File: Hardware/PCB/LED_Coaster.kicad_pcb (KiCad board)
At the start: 2 copper layers, 90 x 90 mm, 67 parts, among them J1 Li-po, J3 USB_C_Receptacle_USB2.0_16P, J4 UART, SW1 SW_SPDT, U1 ESP32-C3-WROOM-02-H4, U3 MCP73831-2-OT, U4 AMS1117-3.3

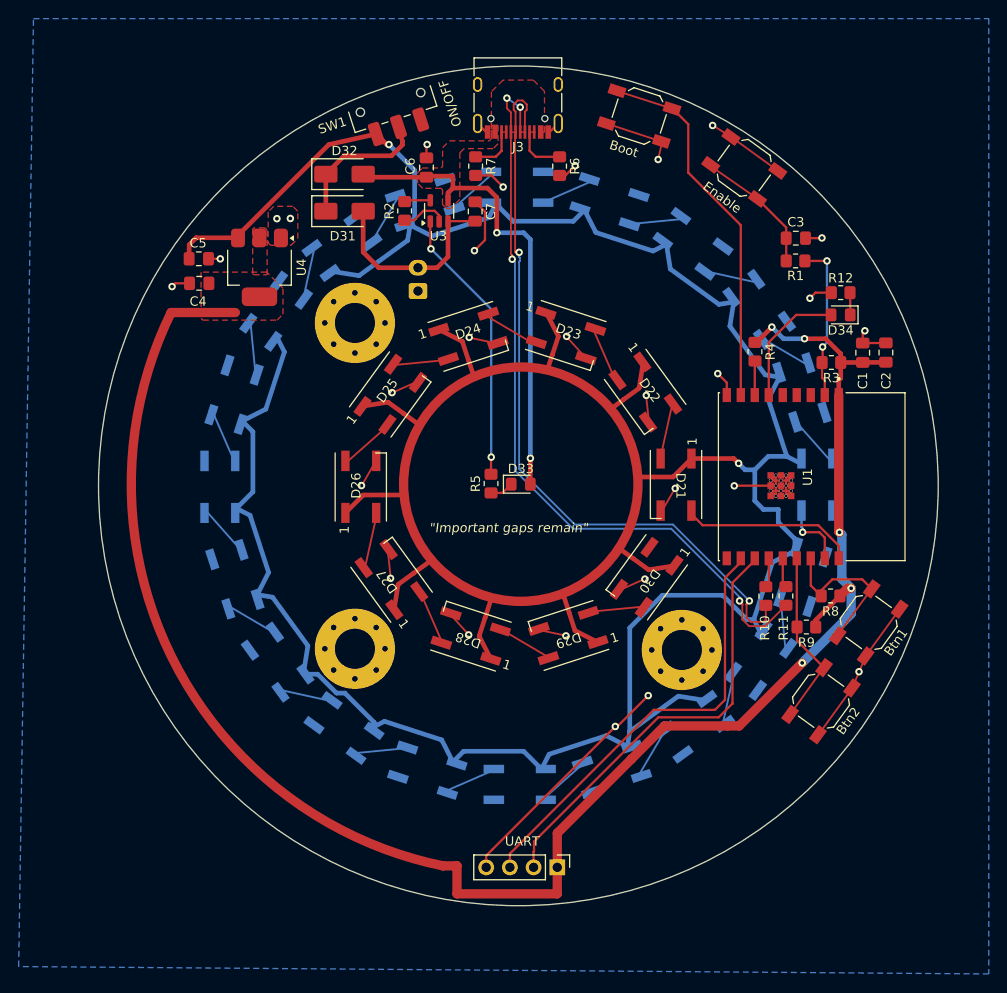
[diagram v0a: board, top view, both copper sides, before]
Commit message: Verify F8 result; correct Phase 3 and rescope Phase 5
Analysed the post-F8 board net by net.

Phase 2 verified: footprint swaps landed, D31/D32 gone, DNP cleared on
D1-D30 and U1 with MPNs intact, 88 parts in both schematic and PCB, and
total copper unchanged at 413 items so no routing was lost. Corrected the
predicted count from 19 added to the actual 23 (C8-C19 were undercounted).

Phase 3 corrected. It said to delete the old +BATT traces feeding the
rings; that would have been destructive. KiCad re-assigned those 104
copper items from +BATT to +LED_PWR automatically during F8 because the
pads they attach to changed net. Only 29 stale items actually need
deleting, all on an empty net in x 129-147, y 42-79.

Phase 5 rescoped: 38 nets need routing, 28 of them LED data links that
were never routed in this file. Confirmed pre-existing by checking the
previous commit - the data nets had zero copper there too.

Decoupling cap advice reversed: 8 of C8-C19 now go on the back beside
their LEDs. The front-only placement existed to avoid double-sided
assembly, which is no longer a constraint.

Co-Authored-By: Claude Opus 5 <noreply@anthropic.com>
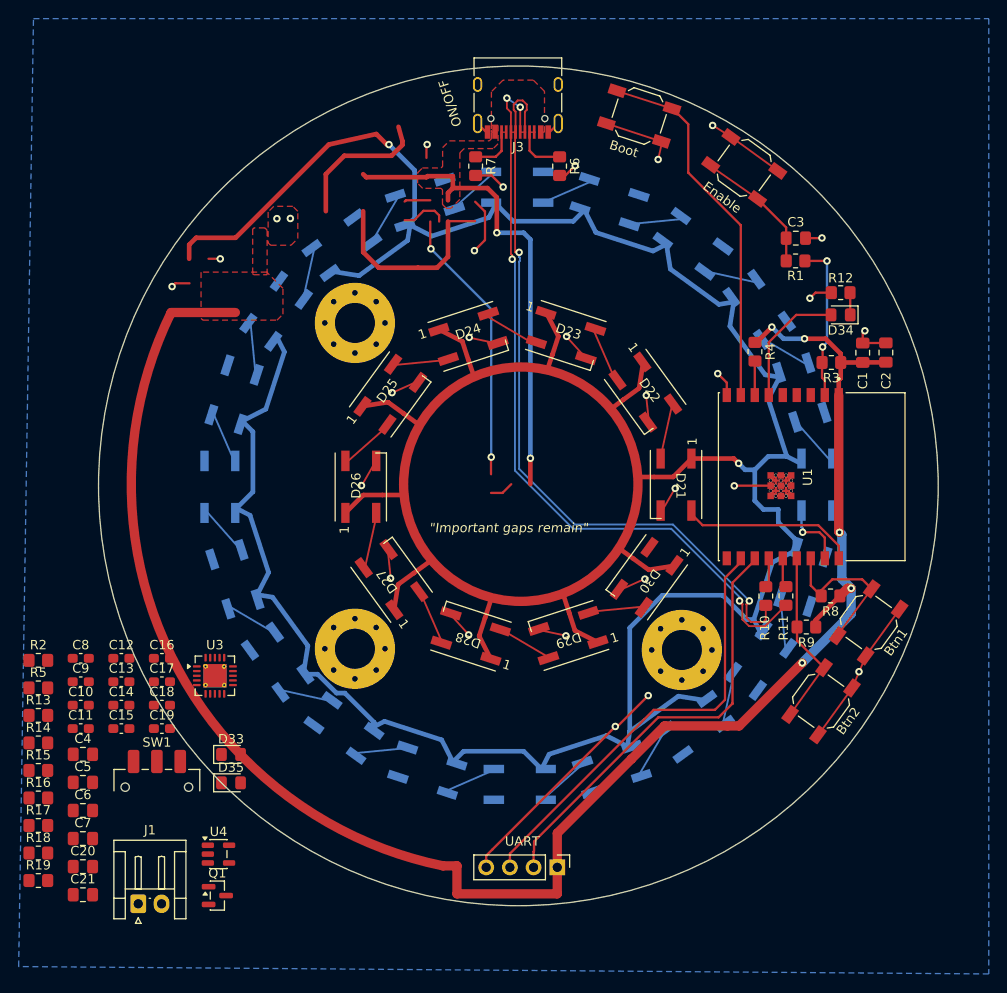
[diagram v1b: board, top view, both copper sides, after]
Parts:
- removed D31, D32: SS34, Diode_SMD:D_SMA
- added C10: 100nF, Capacitor_SMD:C_0603_1608Metric_Pad1.08x0.95mm_HandSolder, F.Cu at (103.1, 103.5)
- added C11: 100nF, Capacitor_SMD:C_0603_1608Metric_Pad1.08x0.95mm_HandSolder, F.Cu at (103.1, 106.0)
- added C12: 100nF, Capacitor_SMD:C_0603_1608Metric_Pad1.08x0.95mm_HandSolder, F.Cu at (107.4, 98.5)
- added C13: 100nF, Capacitor_SMD:C_0603_1608Metric_Pad1.08x0.95mm_HandSolder, F.Cu at (107.4, 101.0)
- added C14: 100nF, Capacitor_SMD:C_0603_1608Metric_Pad1.08x0.95mm_HandSolder, F.Cu at (107.4, 103.5)
- added C15: 100nF, Capacitor_SMD:C_0603_1608Metric_Pad1.08x0.95mm_HandSolder, F.Cu at (107.4, 106.0)
- added C16: 100nF, Capacitor_SMD:C_0603_1608Metric_Pad1.08x0.95mm_HandSolder, F.Cu at (111.8, 98.5)
- added C17: 100nF, Capacitor_SMD:C_0603_1608Metric_Pad1.08x0.95mm_HandSolder, F.Cu at (111.8, 101.0)
- added C18: 100nF, Capacitor_SMD:C_0603_1608Metric_Pad1.08x0.95mm_HandSolder, F.Cu at (111.8, 103.5)
- added C19: 100nF, Capacitor_SMD:C_0603_1608Metric_Pad1.08x0.95mm_HandSolder, F.Cu at (111.8, 106.0)
- added C20: 22uF, Capacitor_SMD:C_0805_2012Metric_Pad1.18x1.45mm_HandSolder, F.Cu at (103.3, 120.8)
- added C21: 0.1uF, Capacitor_SMD:C_0805_2012Metric_Pad1.18x1.45mm_HandSolder, F.Cu at (103.3, 123.8)
- added C8: 100nF, Capacitor_SMD:C_0603_1608Metric_Pad1.08x0.95mm_HandSolder, F.Cu at (103.1, 98.5)
- added C9: 100nF, Capacitor_SMD:C_0603_1608Metric_Pad1.08x0.95mm_HandSolder, F.Cu at (103.1, 101.0)
- added D35: LED, LED_SMD:LED_0805_2012Metric_Pad1.15x1.40mm_HandSolder, F.Cu at (119.2, 111.8)
- added Q1: AO3401A, Package_TO_SOT_SMD:SOT-23, F.Cu at (117.7, 123.9)
- added R13: 100k, Resistor_SMD:R_0805_2012Metric_Pad1.20x1.40mm_HandSolder, F.Cu at (98.5, 104.6)
- added R14: 10k, Resistor_SMD:R_0805_2012Metric_Pad1.20x1.40mm_HandSolder, F.Cu at (98.5, 107.6)
- added R15: 20k, Resistor_SMD:R_0805_2012Metric_Pad1.20x1.40mm_HandSolder, F.Cu at (98.5, 110.5)
- added R16: 1k, Resistor_SMD:R_0805_2012Metric_Pad1.20x1.40mm_HandSolder, F.Cu at (98.5, 113.5)
- added R17: 100k, Resistor_SMD:R_0805_2012Metric_Pad1.20x1.40mm_HandSolder, F.Cu at (98.5, 116.4)
- added R18: 470k, Resistor_SMD:R_0805_2012Metric_Pad1.20x1.40mm_HandSolder, F.Cu at (98.5, 119.4)
- added R19: 470k, Resistor_SMD:R_0805_2012Metric_Pad1.20x1.40mm_HandSolder, F.Cu at (98.5, 122.3)
- C4: value 2.2uF -> 4.7uF
- J1: moved to F.Cu
- U3: value MCP73831-2-OT -> MCP73871-2CC; footprint Package_TO_SOT_SMD:SOT-23-5 -> Package_DFN_QFN:QFN-20-1EP_4x4mm_P0.5mm_EP2.5x2.5mm_ThermalVias
- U4: value AMS1117-3.3 -> TLV75533PDBVR; footprint Package_TO_SOT_SMD:SOT-223-3_TabPin2 -> Package_TO_SOT_SMD:SOT-23-5
- moved C7 79.3 mm to (103.3, 117.8), turned to 0 degrees
- moved C6 78.1 mm to (103.3, 114.8), turned to 0 degrees
- moved SW1 77.6 mm to (111.3, 112.3), turned to 0 degrees
- moved J1 72.2 mm to (109.3, 124.8), turned to 0 degrees
- moved U4 63.0 mm to (117.9, 119.5), turned to 0 degrees
- moved R2 62.1 mm to (98.5, 98.7), turned to 0 degrees
- moved U3 55.3 mm to (117.5, 100.4), turned to 0 degrees
- moved C5 54.9 mm to (103.3, 111.8)
- moved C4 54.5 mm to (103.3, 108.8), turned to 0 degrees
- moved R5 53.2 mm to (98.5, 101.7), turned to 0 degrees
- moved D33 42.5 mm to (119.2, 108.8)
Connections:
- C4 pad 1: GND -> +SYS
- C4 pad 2: +BATT -> GND
- C5 pad 1: GND -> +3V3
- C5 pad 2: +3V3 -> GND
- C6 pad 1: GND -> +5V
- C6 pad 2: +5V -> GND
- C7 pad 1: GND -> +BATT
- C7 pad 2: Net-(D31-A) -> GND
- D1 pad 1: +BATT -> +LED_PWR
- D10 pad 1: +BATT -> +LED_PWR
- D11 pad 1: +BATT -> +LED_PWR
- D12 pad 1: +BATT -> +LED_PWR
- D13 pad 1: +BATT -> +LED_PWR
- D14 pad 1: +BATT -> +LED_PWR
- D15 pad 1: +BATT -> +LED_PWR
- D16 pad 1: +BATT -> +LED_PWR
- D17 pad 1: +BATT -> +LED_PWR
- D18 pad 1: +BATT -> +LED_PWR
- D19 pad 1: +BATT -> +LED_PWR
- D2 pad 1: +BATT -> +LED_PWR
- D20 pad 1: +BATT -> +LED_PWR
- D21 pad 1: +BATT -> +LED_PWR
- D22 pad 1: +BATT -> +LED_PWR
- D23 pad 1: +BATT -> +LED_PWR
- D24 pad 1: +BATT -> +LED_PWR
- D25 pad 1: +BATT -> +LED_PWR
- D26 pad 1: +BATT -> +LED_PWR
- D27 pad 1: +BATT -> +LED_PWR
- D28 pad 1: +BATT -> +LED_PWR
- D29 pad 1: +BATT -> +LED_PWR
- D3 pad 1: +BATT -> +LED_PWR
- D30 pad 1: +BATT -> +LED_PWR
- D4 pad 1: +BATT -> +LED_PWR
- D5 pad 1: +BATT -> +LED_PWR
- D6 pad 1: +BATT -> +LED_PWR
- D7 pad 1: +BATT -> +LED_PWR
- D8 pad 1: +BATT -> +LED_PWR
- D9 pad 1: +BATT -> +LED_PWR
- J1 pad 2: Net-(D31-A) -> +BATT
- R2 pad 1: Net-(U3-PROG) -> Net-(U3-PROG1)
- R2 pad 2: Net-(U3-V_{SS}) -> GND
- R5 pad 1: Net-(D33-K) -> Net-(U3-STAT1/~{LBO})
- R5 pad 2: Net-(U3-STAT) -> Net-(D33-K)
- SW1 pad 2: Net-(D31-K) -> GND
- SW1 pad 3: +BATT -> Net-(Q1-G)
- U1 pad 3: unconnected-(U1-IO4-Pad3) -> /BAT_SENSE
- U3 pad 1: Net-(U3-STAT) -> +SYS
- U3 pad 2: Net-(U3-V_{SS}) -> +5V
- U3 pad 3: Net-(D31-A) -> GND
- U3 pad 4: +5V -> +SYS
- U3 pad 5: Net-(U3-PROG) -> Net-(U3-THERM)
- U4 pad 1: GND -> +SYS
- U4 pad 2: +3V3 -> GND
- U4 pad 3: +BATT -> +LED_PWR
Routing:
- net +LED_PWR: track 0.00 -> 318.8 mm, vias 0 -> 2
- net +BATT: track 318.8 -> 0.00 mm, vias 2 -> 0
- net (no net): track 0.00 -> 74.4 mm, vias 0 -> 2
- net Net-(U3-STAT): track 29.8 -> 0.00 mm, vias 2 -> 0
- net Net-(D31-A): track 21.4 -> 0.00 mm
- net Net-(D31-K): track 15.5 -> 0.00 mm
- net Net-(U3-V_{SS}): track 4.98 -> 0.00 mm
- net Net-(U3-PROG): track 2.80 -> 0.00 mm

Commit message: Phase 3: delete the orphaned copper from the old power section
The 29 netless copper items left behind by D31/D32 and the old U3/U4
footprints are removed. Total board copper goes 413 -> 384; nothing else
changed. +LED_PWR keeps its 104-item ring distribution, GND 92, the ring
inputs, USB and buttons untouched, 88 footprints, antenna keepout intact.
No netless copper remains.

ORDERING.md corrections found while verifying readiness:

- Phase 3 lists the exact bounding box and the 25 F.Cu / 2 via / 2 B.Cu
  breakdown, and now says to select by net rather than rubber-banding an
  area that also holds live +5V, GND and +LED_PWR copper. A new box says
  to leave the netless ESP32 antenna keepout zone alone.
- Phase 4 said "SW1 - leave it where it is". F8 moved the entire power
  section off the board, SW1 included, because the section was redrawn in
  the schematic. Phase 4 now lists the 28 off-board footprints and the
  pre-F8 positions worth reusing, and gains placement boxes for J1 and
  D33, which it previously referenced but never told you to place.
- Phase 8 expected 27 BOM lines; the schematic yields 26 for 83 parts.
- The v10 format upgrade box is ticked - it landed inside e196df2.

Co-Authored-By: Claude Opus 5 <noreply@anthropic.com>
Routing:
- net (no net): track 74.4 -> 0.00 mm, vias 2 -> 0

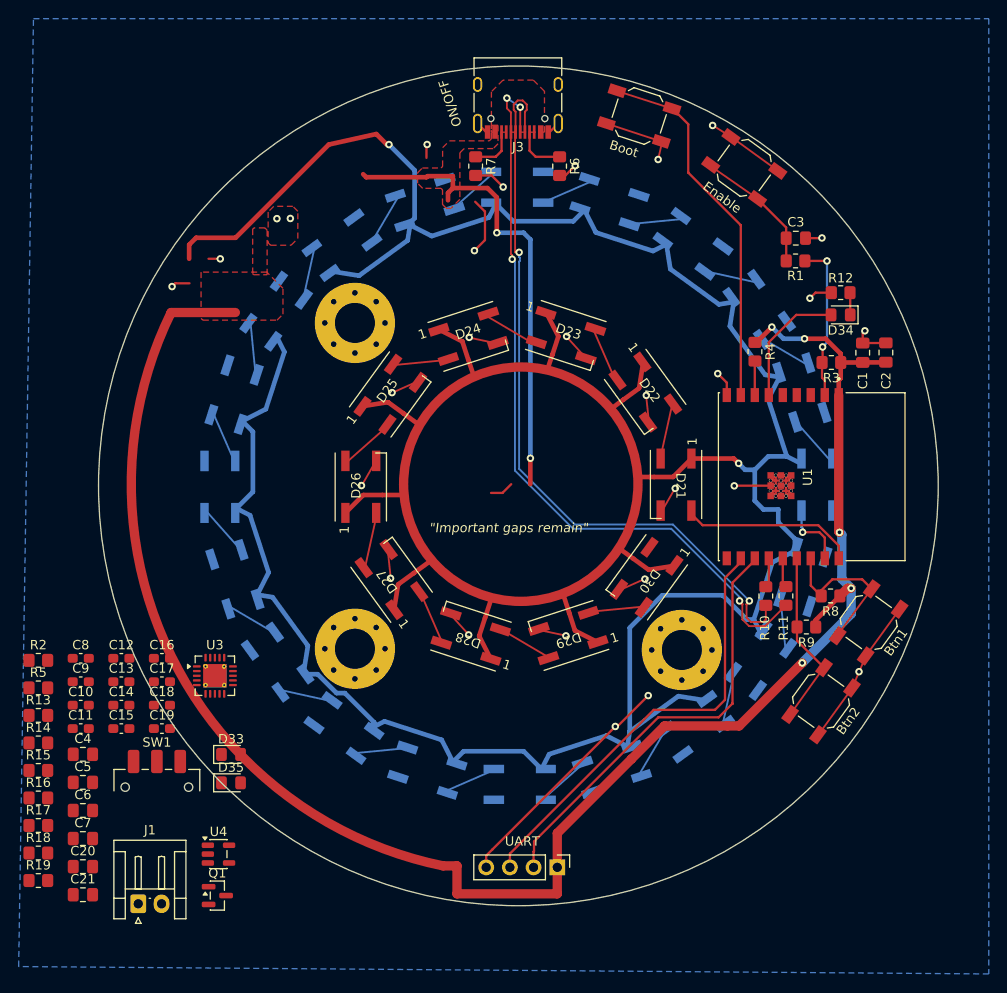
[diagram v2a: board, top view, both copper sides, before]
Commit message: Phase 4: place all 34 parts, and correct the outer-ring rotation analysis
Every unplaced part now has a verified position, angle and side. Checked
against the board file: courtyard overlap per side, through-hole pads against
the opposite side, all four corners inside the 90 mm outline, and every pad
against tracks of a foreign net.

Before placing, 13 more leftovers went: 7 thin +LED_PWR feed segments from the
old switch run and 4 GND segments plus 2 vias from the old C4/C5 connections.
Phase 3 could not catch these because they still carried a live net. Copper is
371 items. Three dead copper zones also went - two +3V3 and one GND, drawn
around the old AMS1117 at (122.25, 56.58), each connecting to zero pads of its
own net and each sitting on top of the new charger. 15 zones remain.

Two placement decisions differ from what this file said before:

- The status LEDs D33/D35 and their resistors moved from the centre of the
  front face to the back, outside the LED ring, 10 mm from the USB-C port. The
  front face is almost hidden in the enclosure.
- The battery-sense divider R18/R19 groups with C21 at the ESP32 rather than at
  the battery, so the 235k divider node stays short and +BATT takes the long
  run instead.

Corrected: the outer ring D1-D20 is not uniformly oriented. An earlier revision
here claimed both rings held their angle to 0.1°, measured with rot + bearing.
That is the right invariant on the front and the wrong one on a mirrored layer.
Measured with rot - bearing the outer ring spreads 324° - it carries front-side
rotations while the parts sit on the back, fanning through 5 orientations 36°
apart. Pre-existing and identical in the previously fabricated board. Not worth
fixing: re-rotating all 20 would give uniform 5.5 mm data hops instead of
4-16 mm, but collides with H1/H3/H4, J1, C10 and C14.

That fan is why the decoupling caps take rot = -bearing on both sides rather
than a radial rule. It holds each cap at a fixed angle to its neighbouring LEDs
- 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
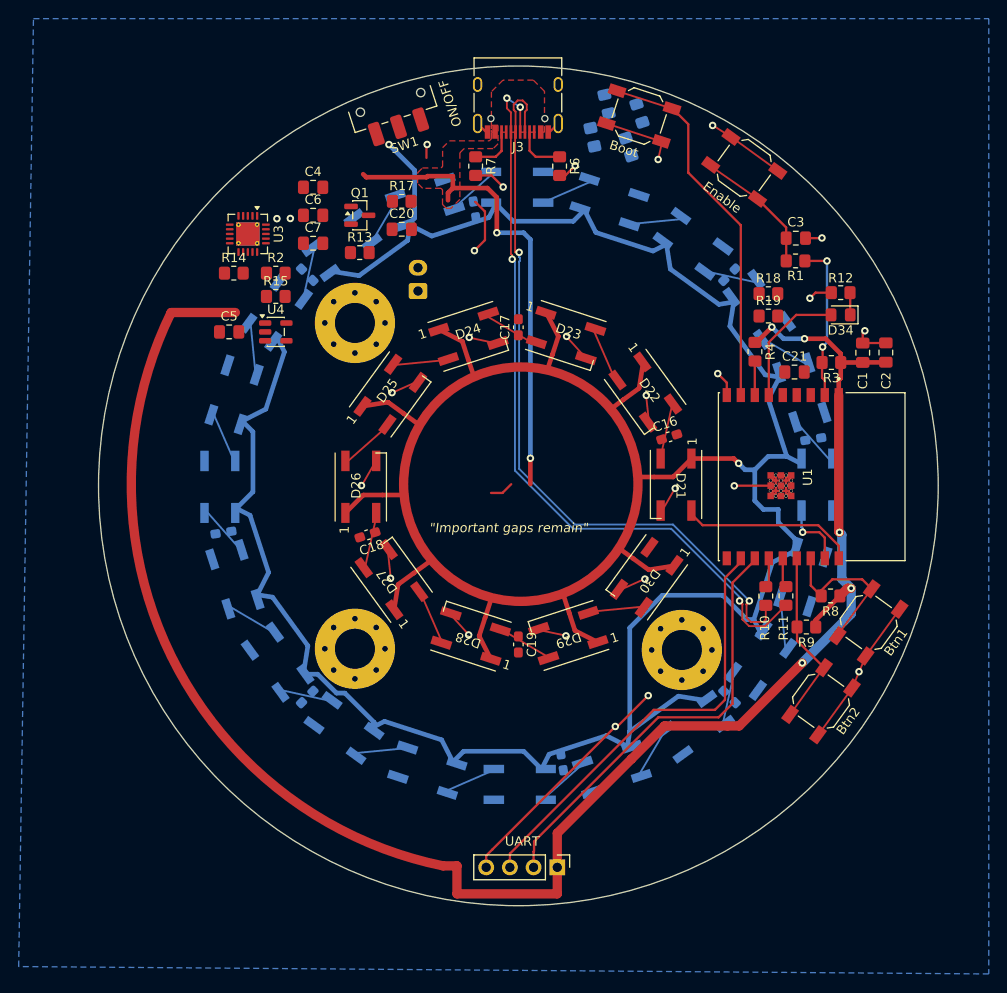
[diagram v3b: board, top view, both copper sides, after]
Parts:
- C10, C11, C12, C13, C14, C15, C8, C9, D33, D35, J1, R16, R5: moved to B.Cu
- moved R19 98.9 mm to (176.8, 61.8)
- moved R18 98.6 mm to (176.8, 59.4)
- moved C21 94.6 mm to (179.6, 67.8)
- moved R16 94.2 mm to (161.8, 43.7), turned to 108 degrees
- moved D35 84.1 mm to (163.0, 40.1), turned to 108 degrees
- moved R5 83.7 mm to (157.9, 42.6), turned to 102 degrees
- moved C9 82.1 mm to (172.6, 57.4), turned to 45 degrees
- moved C8 82.0 mm to (181.6, 75.0), turned to 9 degrees
- moved D33 80.5 mm to (159.4, 39.1), turned to 103 degrees
- moved SW1 77.6 mm to (136.3, 38.9), turned to -162 degrees
- moved R17 77.4 mm to (137.5, 49.5)
- moved C20 76.4 mm to (137.5, 52.5)
- moved Q1 74.5 mm to (133.0, 51.0)
- moved J1 72.2 mm to (139.2, 59.1), turned to 90 degrees
- moved C7 68.4 mm to (128.0, 54.0)
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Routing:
- net +LED_PWR: track 318.8 -> 290.8 mm
- net GND: track 76.9 -> 73.6 mm, vias 28 -> 26
- removed copper zone on F.Cu, net +3V3
- removed copper zone on F.Cu, net GND
